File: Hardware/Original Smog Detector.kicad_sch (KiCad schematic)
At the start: 0 parts

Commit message: Redrew the original circuit without the battery, switch and output jack
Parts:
- added AE1: Antenna_Shield, symbol Device:Antenna_Shield
- added C1: 10n, symbol Device:C
- added C2, C3, C4: C_Polarized 10µF 16V, symbol Device:C_Polarized
- added D1: BAT54S, Package_TO_SOT_SMD:SOT-23, symbol Diode:BAT54S
- added Q1: Q_NPN_BEC BSR17A, symbol Device:Q_NPN_BEC
- added Q2, Q3: BC547, Package_TO_SOT_THT:TO-92_Inline, symbol Transistor_BJT:BC547
- added R2, R3: 10k, symbol Device:R
- added R2, R4: 100k, symbol Device:R
- added R5: 1k, symbol Device:R
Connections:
- new net: C3.1, R2.2, R4.1
- new net: AE1.1 (A), C1.1, D1.3 (COM)
- new net: C4.1, Q3.1 (C), R4.2, R5.2
- new net: C1.2, Q1.1 (B), R2.1
- new net: Q1.3 (C), Q2.2 (B), R2.2
- new net: Q2.1 (C), Q3.2 (B), R3.2
- new net +1V5: C2.1, R2.1, R3.1, R5.1
- new net GND: AE1.2 (Shield), C2.2, C3.2, D1.1 (A), D1.2 (K), Q1.2 (E), Q2.3 (E), Q3.3 (E)

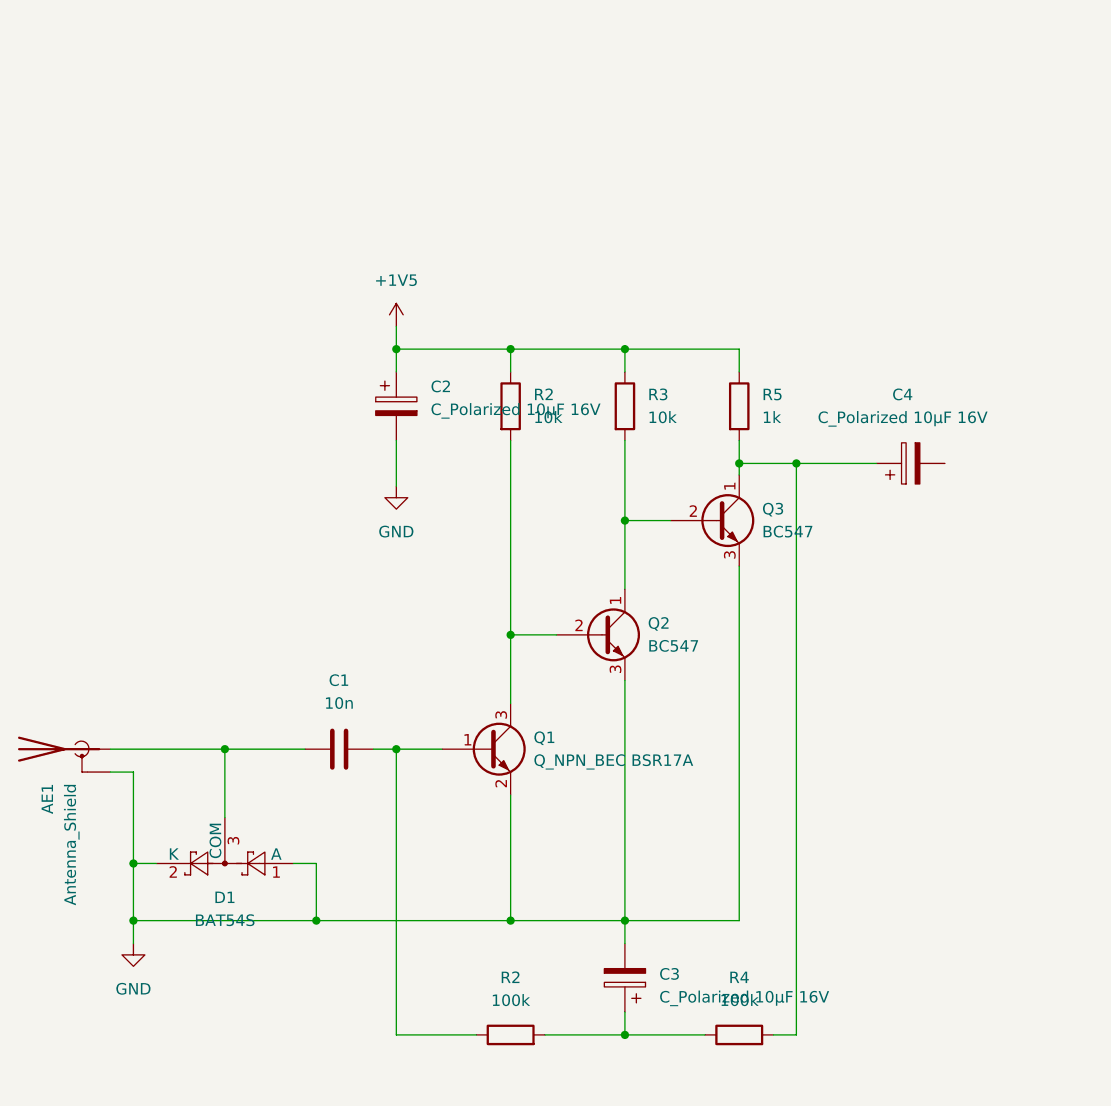
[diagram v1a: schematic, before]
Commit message: Changed power labels to hierarchical labels and DC coupled the output
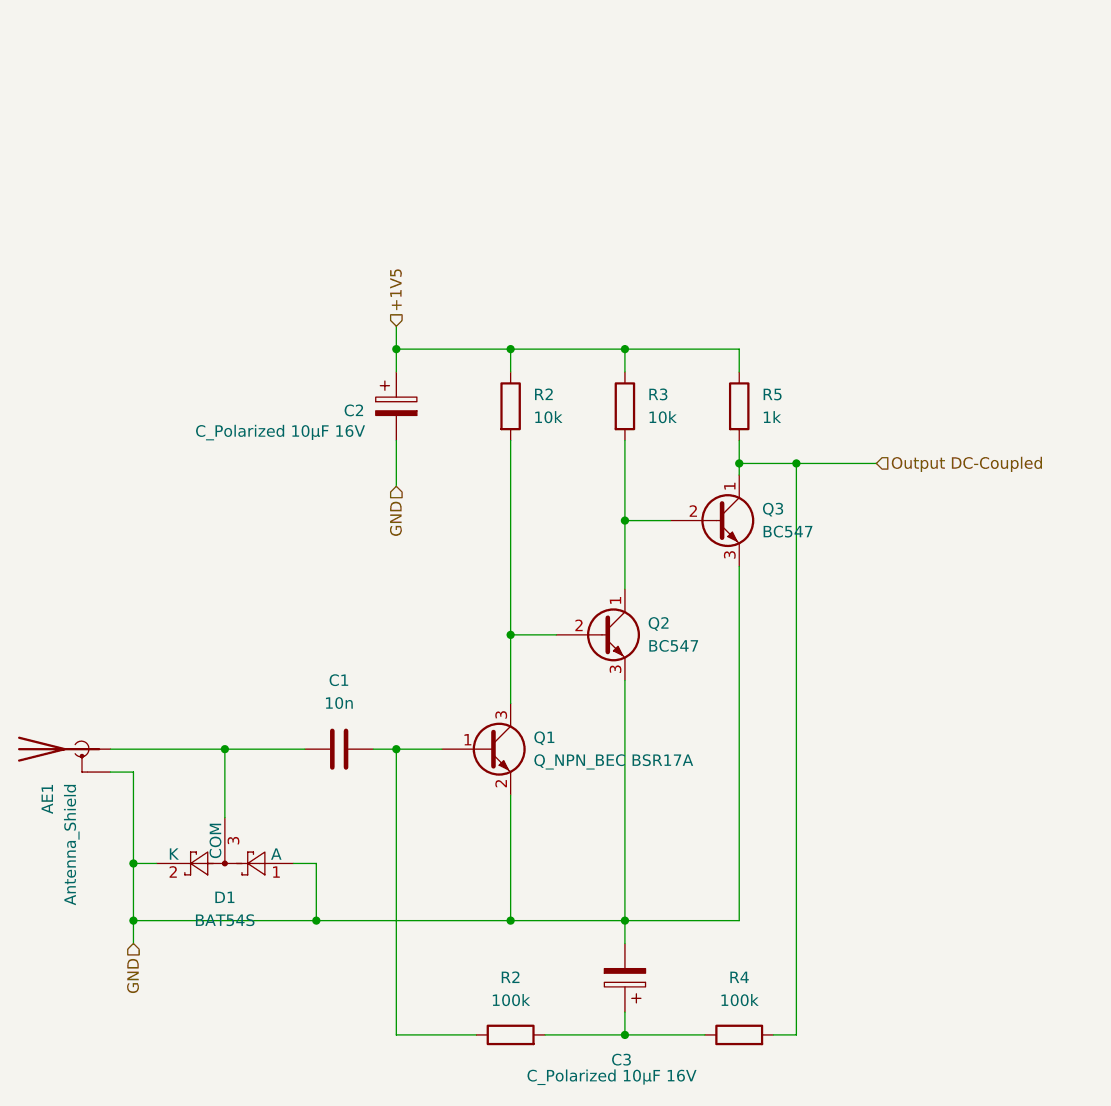
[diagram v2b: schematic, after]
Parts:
- removed C4: C_Polarized 10µF 16V, symbol Device:C_Polarized
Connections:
- net Output DC-Coupled: now reaches Q3.1 (C), R4.2, R5.2

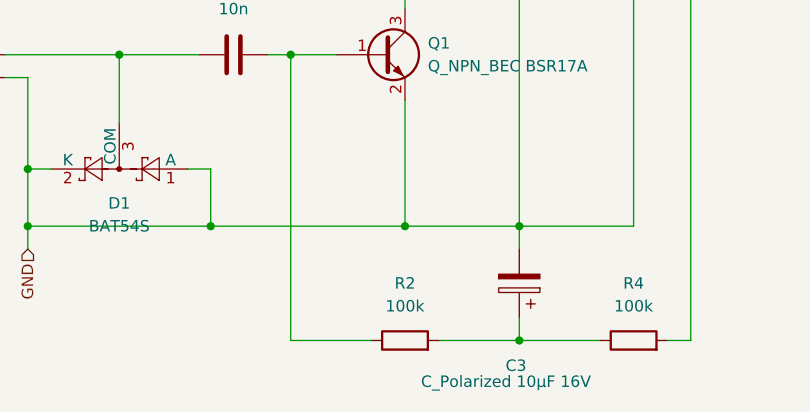
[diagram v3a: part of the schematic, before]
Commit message: changed duplicate resistor reference designator from R2 to R17
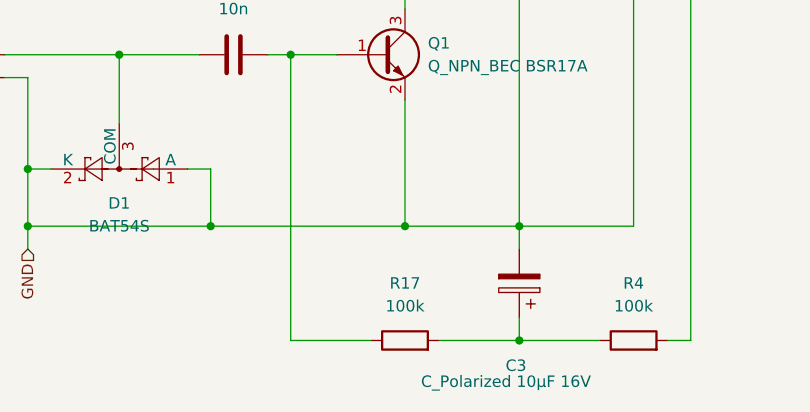
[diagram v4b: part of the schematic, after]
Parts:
- renumbered R2 to R17
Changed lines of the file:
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@@
 		(dnp no)
 		(fields_autoplaced yes)
-		(property "Reference" "R2"
+		(property "Reference" "R17"
 			(at 101.6 120.65 90)
 			(effects
@@
 			(project ""
 				(path "/4e457c11-25d4-4677-9942-6ed7396aaf8a/154ccd26-fdda-4c85-b8a7-c0bf9df9e351"
-					(reference "R2")
+					(reference "R17")
 					(unit 1)
 				)

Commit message: Started linking footprints and work on the pcb layout
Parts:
- C1, C2: footprint (none) -> Capacitor_SMD:C_0805_2012Metric_Pad1.18x1.45mm_HandSolder
- Q1: footprint (none) -> Package_TO_SOT_SMD:SOT-23
- R17, R2, R3, R4, R5: footprint (none) -> Resistor_SMD:R_0402_1005Metric_Pad0.72x0.64mm_HandSolder
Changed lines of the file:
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@@
 			)
 		)
-		(property "Footprint" ""
+		(property "Footprint" "Resistor_SMD:R_0402_1005Metric_Pad0.72x0.64mm_HandSolder"
 			(at 127 128.778 90)
 			(effects
@@
 			)
 		)
-		(property "Footprint" ""
+		(property "Footprint" "Capacitor_SMD:C_0805_2012Metric_Pad1.18x1.45mm_HandSolder"
 			(at 86.36 94.2848 0)
 			(effects
@@
 			)
 		)
-		(property "Footprint" ""
+		(property "Footprint" "Resistor_SMD:R_0402_1005Metric_Pad0.72x0.64mm_HandSolder"
 			(at 99.822 57.15 90)
 			(effects
@@
 			)
 		)
-		(property "Footprint" ""
+		(property "Footprint" "Resistor_SMD:R_0402_1005Metric_Pad0.72x0.64mm_HandSolder"
 			(at 125.222 57.15 90)
 			(effects
@@
 			)
 		)
-		(property "Footprint" ""
+		(property "Footprint" "Package_TO_SOT_SMD:SOT-23"
 			(at 104.14 92.71 0)
 			(effects
@@
 			)
 		)
-		(property "Datasheet" "~"
+		(property "Datasheet" "https://www.onsemi.com/download/data-sheet/pdf/bsr17a-d.pdf"
 			(at 99.06 95.25 0)
 			(effects
@@
 			)
 		)
-		(property "Footprint" ""
+		(property "Footprint" "Resistor_SMD:R_0402_1005Metric_Pad0.72x0.64mm_HandSolder"
 			(at 101.6 128.778 90)
 			(effects
@@
 			)
 		)
-		(property "Footprint" ""
+		(property "Footprint" "Resistor_SMD:R_0402_1005Metric_Pad0.72x0.64mm_HandSolder"
 			(at 112.522 57.15 90)
 			(effects
@@
 			)
 		)
-		(property "Footprint" ""
+		(property "Footprint" "Capacitor_SMD:C_0805_2012Metric_Pad1.18x1.45mm_HandSolder"
 			(at 89.8652 60.96 0)
 			(effects

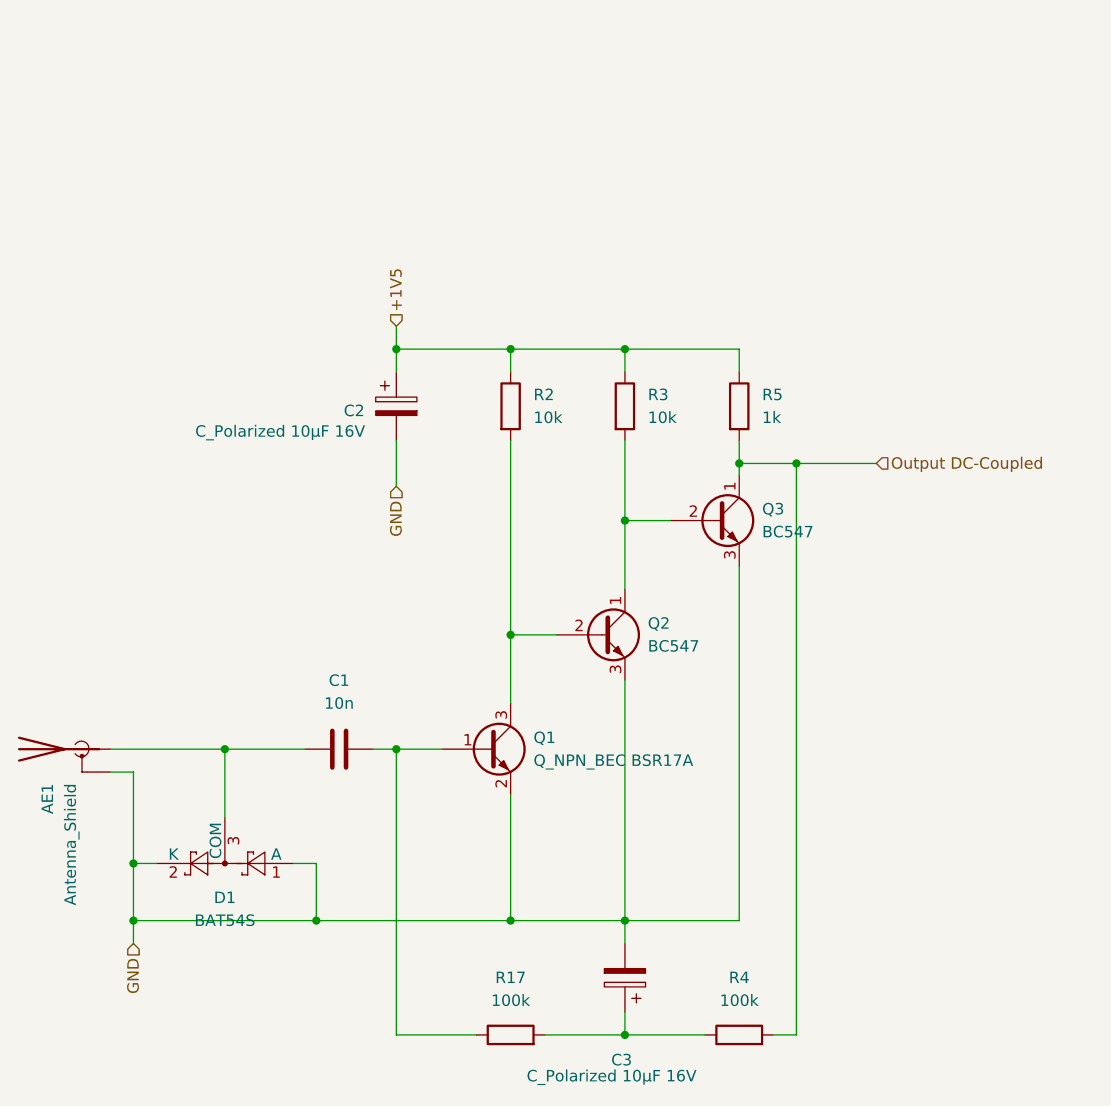
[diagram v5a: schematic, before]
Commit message: added more footprints and continued on the circuit diagram
- [ ] add antenna connection
- [ ] find suitable 390Mohm resistor
- [ ] add switches, reset and power
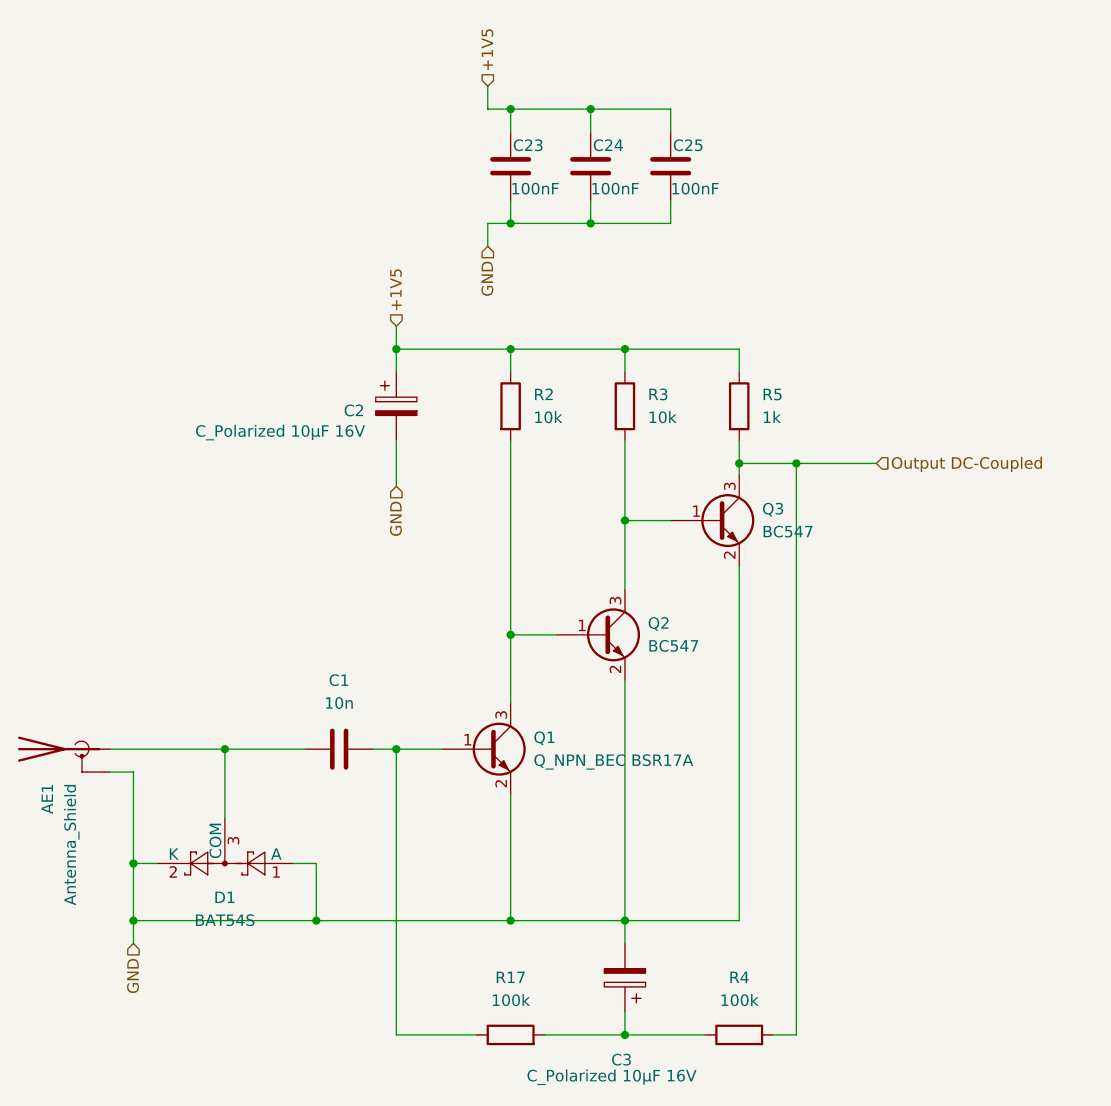
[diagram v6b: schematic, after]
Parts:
- added C23, C24, C25: 100nF, Capacitor_SMD:C_0402_1005Metric_Pad0.74x0.62mm_HandSolder, symbol Device:C
- Q2, Q3: footprint Package_TO_SOT_THT:TO-92_Inline -> Package_TO_SOT_SMD:SOT-23; symbol Transistor_BJT:BC547 -> Transistor_BJT:BC847
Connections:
- net +1V5: now also C23.1, C24.1, C25.1
- net GND: now also Q2.2 (E), Q3.2 (E), C23.2, C24.2, C25.2; no longer Q2.3 (E), Q3.3 (E)
- net Output DC-Coupled: now also Q3.3 (C); no longer Q3.1 (C)
- net at Q1.3 (C), R2.2: now also Q2.1 (B); no longer Q2.2 (B)
- new net: Q2.3 (C), Q3.1 (B), R3.2

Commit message: PCB is done???
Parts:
- AE1: footprint (none) -> Connector_PinHeader_2.54mm:PinHeader_1x02_P2.54mm_Vertical_SMD_Pin1Left
- C3: footprint (none) -> Capacitor_SMD:C_0805_2012Metric_Pad1.18x1.45mm_HandSolder
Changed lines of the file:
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@@
 			)
 		)
-		(property "Footprint" ""
+		(property "Footprint" "Capacitor_SMD:C_0805_2012Metric_Pad1.18x1.45mm_HandSolder"
 			(at 113.3348 116.84 0)
 			(effects
@@
 			)
 		)
-		(property "Footprint" ""
+		(property "Footprint" "Connector_PinHeader_2.54mm:PinHeader_1x02_P2.54mm_Vertical_SMD_Pin1Left"
 			(at 49.53 95.25 0)
 			(effects
